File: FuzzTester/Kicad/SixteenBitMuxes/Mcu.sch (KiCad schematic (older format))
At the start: 20 parts, among them J10 Key Pad JST XH, J11 LCD JST XH, J12 Bypass Switch JST XH, J7 Boot Reset PinHeader, J8 SPI Test PinHeader, J9 SWD_PinHeader, U3 STM32F103C8Tx, Y1 8MHz

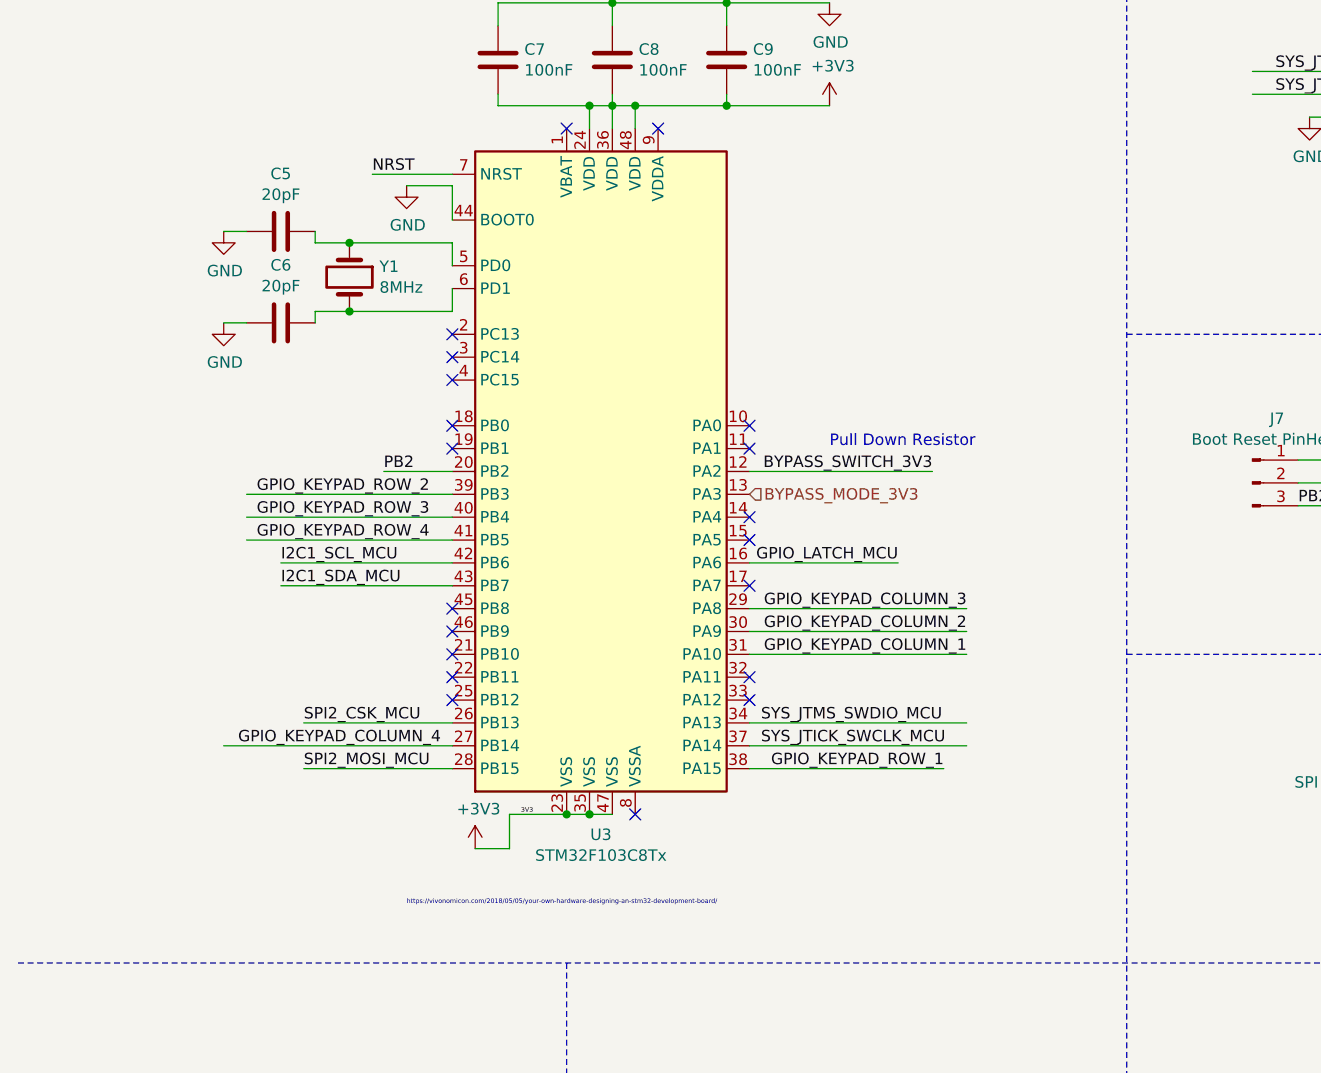
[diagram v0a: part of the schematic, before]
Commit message: Removed shift registers
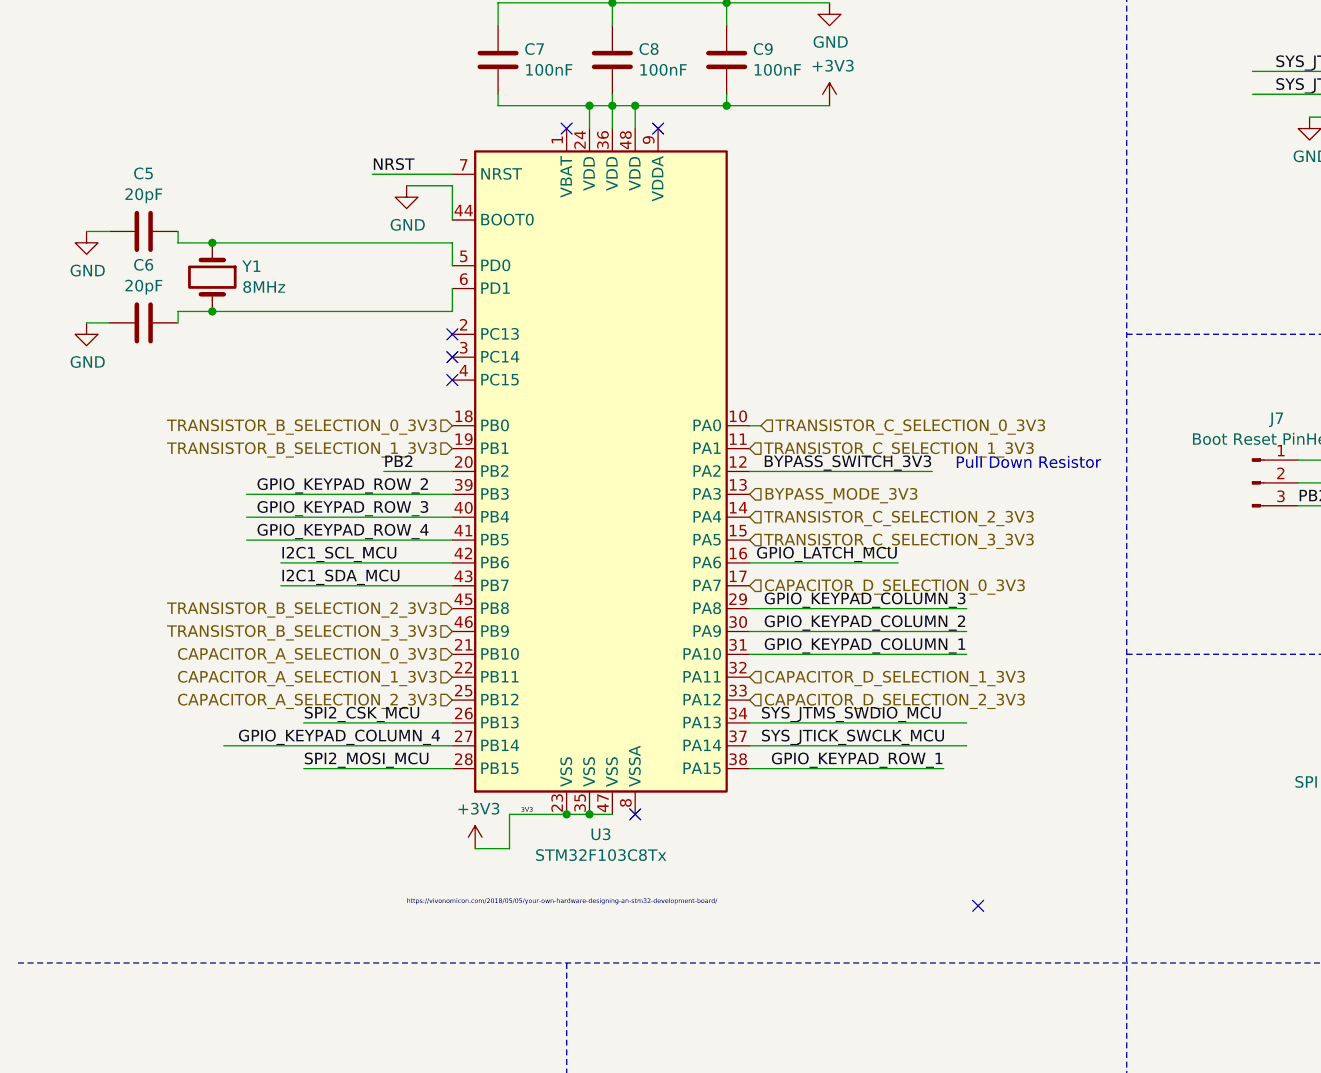
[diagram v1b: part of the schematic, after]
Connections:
- net labels added: CAPACITOR_A_SELECTION_0_3V3, CAPACITOR_A_SELECTION_1_3V3, CAPACITOR_A_SELECTION_2_3V3, CAPACITOR_D_SELECTION_0_3V3, CAPACITOR_D_SELECTION_1_3V3, CAPACITOR_D_SELECTION_2_3V3, TRANSISTOR_B_SELECTION_0_3V3, TRANSISTOR_B_SELECTION_1_3V3, TRANSISTOR_B_SELECTION_2_3V3, TRANSISTOR_B_SELECTION_3_3V3, TRANSISTOR_C_SELECTION_0_3V3, TRANSISTOR_C_SELECTION_1_3V3, TRANSISTOR_C_SELECTION_2_3V3, TRANSISTOR_C_SELECTION_3_3V3
- wire segments 93 -> 94
- no-connect marks 22 -> 9
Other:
- moved on the sheet: C5, C6, Y1
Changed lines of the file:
@@
 $Descr A4 11693 8268
 encoding utf-8
-Sheet 11 11
+Sheet 6 9
 Title "Guitar Pedal Effect Fuzz Digitally Controlled"
 Date "2020-04-07"
@@
 Comment4 "Micro Controller Unit and User Interface"
 $EndDescr
-$Comp
-L MCU_ST_STM32F1:STM32F103C8Tx U?
-U 1 1 5E8CE625
-P 3100 3050
-AR Path="/5E8CE625" Ref="U?"  Part="1"
-AR Path="/5E8BDF21/5E8CE625" Ref="U3"  Part="1"
-F 0 "U3" H 3050 1461 50  0000 C CNN
-F 1 "STM32F103C8Tx" H 3050 1370 50  0000 C CNN
-F 2 "Package_QFP:LQFP-48_7x7mm_P0.5mm" H 2500 1650 50  0001 R CNN
-F 3 "http://www.st.com/st-web-ui/static/active/en/resource/technical/document/datasheet/CD00161566.pdf" H 3100 3050 50  0001 C CNN
-	1    3100 3050
-	1    0    0    -1
-$EndComp
 $Comp
 L Device:C C?
@@
 Wire Wire Line
 	2650 4700 2650 4550
-Wire Wire Line
-	2900 4550 3000 4550
-Connection ~ 3000 4550
-Wire Wire Line
-	3000 4550 3100 4550
 Text Label 2700 4550 0    20   ~ 0
 3V3
@@
 L Device:Crystal Y?
 U 1 1 5E8CE662
-P 1950 2200
+P 1350 2200
 AR Path="/5E8CE662" Ref="Y?"  Part="1"
 AR Path="/5E8BDF21/5E8CE662" Ref="Y1"  Part="1"
-F 0 "Y1" V 1904 2331 50  0000 L CNN
-F 1 "8MHz" V 1995 2331 50  0000 L CNN
-F 2 "Crystal:Crystal_HC49-U_Vertical" H 1950 2200 50  0001 C CNN
-F 3 "~" H 1950 2200 50  0001 C CNN
-	1    1950 2200
+F 0 "Y1" V 1304 2331 50  0000 L CNN
+F 1 "8MHz" V 1395 2331 50  0000 L CNN
+F 2 "Crystal:Crystal_HC49-U_Vertical" H 1350 2200 50  0001 C CNN
+F 3 "~" H 1350 2200 50  0001 C CNN
+	1    1350 2200
 	0    1    1    0
 $EndComp
@@
 L Device:C C?
 U 1 1 5E8CE668
-P 1650 2000
+P 1050 2000
 AR Path="/5E8CE668" Ref="C?"  Part="1"
 AR Path="/5E8BDF21/5E8CE668" Ref="C5"  Part="1"
-F 0 "C5" V 1398 2000 50  0000 C CNN
-F 1 "20pF" V 1489 2000 50  0000 C CNN
-F 2 "Capacitor_SMD:C_0805_2012Metric_Pad1.15x1.40mm_HandSolder" H 1688 1850 50  0001 C CNN
-F 3 "~" H 1650 2000 50  0001 C CNN
-	1    1650 2000
+F 0 "C5" V 798 2000 50  0000 C CNN
+F 1 "20pF" V 889 2000 50  0000 C CNN
+F 2 "Capacitor_SMD:C_0805_2012Metric_Pad1.15x1.40mm_HandSolder" H 1088 1850 50  0001 C CNN
+F 3 "~" H 1050 2000 50  0001 C CNN
+	1    1050 2000
 	0    1    1    0
 $EndComp
@@
 L Device:C C?
 U 1 1 5E8CE66E
-P 1650 2400
+P 1050 2400
 AR Path="/5E8CE66E" Ref="C?"  Part="1"
 AR Path="/5E8BDF21/5E8CE66E" Ref="C6"  Part="1"
-F 0 "C6" V 1398 2400 50  0000 C CNN
-F 1 "20pF" V 1489 2400 50  0000 C CNN
-F 2 "Capacitor_SMD:C_0805_2012Metric_Pad1.15x1.40mm_HandSolder" H 1688 2250 50  0001 C CNN
-F 3 "~" H 1650 2400 50  0001 C CNN
-	1    1650 2400
+F 0 "C6" V 798 2400 50  0000 C CNN
+F 1 "20pF" V 889 2400 50  0000 C CNN
+F 2 "Capacitor_SMD:C_0805_2012Metric_Pad1.15x1.40mm_HandSolder" H 1088 2250 50  0001 C CNN
+F 3 "~" H 1050 2400 50  0001 C CNN
+	1    1050 2400
 	0    1    1    0
 $EndComp
@@
 	2400 2250 2400 2350
 Wire Wire Line
-	2400 2350 1950 2350
-Wire Wire Line
-	1800 2400 1800 2350
-Wire Wire Line
-	1800 2350 1950 2350
-Connection ~ 1950 2350
-Wire Wire Line
-	1800 2000 1800 2050
-Wire Wire Line
-	1800 2050 1950 2050
-Wire Wire Line
-	1950 2050 2400 2050
+	1200 2400 1200 2350
+Wire Wire Line
+	1200 2350 1350 2350
+Connection ~ 1350 2350
+Wire Wire Line
+	1200 2000 1200 2050
+Wire Wire Line
+	1200 2050 1350 2050
 Wire Wire Line
 	2400 2050 2400 2150
-Connection ~ 1950 2050
+Connection ~ 1350 2050
 $Comp
 L power:GND #PWR?
 U 1 1 5E8CE67E
-P 1400 2400
+P 800 2400
 AR Path="/5E8CE67E" Ref="#PWR?"  Part="1"
 AR Path="/5E8BDF21/5E8CE67E" Ref="#PWR018"  Part="1"
-F 0 "#PWR018" H 1400 2150 50  0001 C CNN
-F 1 "GND" H 1405 2227 50  0000 C CNN
-F 2 "" H 1400 2400 50  0001 C CNN
-F 3 "" H 1400 2400 50  0001 C CNN
-	1    1400 2400
+F 0 "#PWR018" H 800 2150 50  0001 C CNN
+F 1 "GND" H 805 2227 50  0000 C CNN
+F 2 "" H 800 2400 50  0001 C CNN
+F 3 "" H 800 2400 50  0001 C CNN
+	1    800  2400
 	1    0    0    -1
 $EndComp
@@
 L power:GND #PWR?
 U 1 1 5E8CE684
-P 1400 2000
+P 800 2000
 AR Path="/5E8CE684" Ref="#PWR?"  Part="1"
 AR Path="/5E8BDF21/5E8CE684" Ref="#PWR017"  Part="1"
-F 0 "#PWR017" H 1400 1750 50  0001 C CNN
-F 1 "GND" H 1405 1827 50  0000 C CNN
-F 2 "" H 1400 2000 50  0001 C CNN
-F 3 "" H 1400 2000 50  0001 C CNN
-	1    1400 2000
-	1    0    0    -1
-$EndComp
-Wire Wire Line
-	1400 2000 1500 2000
-Wire Wire Line
-	1400 2400 1500 2400
+F 0 "#PWR017" H 800 1750 50  0001 C CNN
+F 1 "GND" H 805 1827 50  0000 C CNN
+F 2 "" H 800 2000 50  0001 C CNN
+F 3 "" H 800 2000 50  0001 C CNN
+	1    800  2000
+	1    0    0    -1
+$EndComp
+Wire Wire Line
+	800  2000 900  2000
+Wire Wire Line
+	800  2400 900  2400
 Wire Wire Line
 	3600 1000 4050 1000
@@
 Wire Wire Line
 	2100 3050 2400 3050
-Wire Wire Line
-	2650 4550 2900 4550
-Connection ~ 2900 4550
 Text Notes 2200 900  0    50   ~ 10
 Micro Controller Unit\n\n\n
@@
 Text Notes 6350 1300 0    50   ~ 10
 SWD\n\n\n
-NoConn ~ 2400 2650
-NoConn ~ 2400 2550
-NoConn ~ 2400 2450
-NoConn ~ 2400 4050
-NoConn ~ 2400 3950
-NoConn ~ 2400 3850
-NoConn ~ 2400 3750
-NoConn ~ 2400 3650
-NoConn ~ 3700 4050
-NoConn ~ 3700 3950
-NoConn ~ 3700 3550
-NoConn ~ 3700 3350
-NoConn ~ 3700 3250
-NoConn ~ 3700 2950
-NoConn ~ 3700 2850
 NoConn ~ 2900 1550
 NoConn ~ 3300 1550
@@
 Wire Wire Line
 	8700 4400 9250 4400
-NoConn ~ 2400 2850
-Text Notes 4050 2950 0    50   ~ 0
+Text Notes 4600 3050 0    50   ~ 0
 Pull Down Resistor
 Text HLabel 3700 3150 2    50   Input ~ 0
@@
 Text Label 2350 4250 2    50   ~ 0
 GPIO_KEYPAD_COLUMN_4
-NoConn ~ 2400 2950
 Text Label 9500 1650 2    50   ~ 0
 GPIO_KEYPAD_ROW_4
@@
 Wire Wire Line
 	1650 3450 2400 3450
-$Comp
-L Device:R_Pack04 RN1
-U 1 1 5EA7B481
-P 1850 6700
-F 0 "RN1" V 1433 6700 50  0000 C CNN
-F 1 "R_Pack04" V 1524 6700 50  0000 C CNN
-F 2 "Resistor_SMD:R_Array_Convex_4x0603" V 2125 6700 50  0001 C CNN
-F 3 "~" H 1850 6700 50  0001 C CNN
-	1    1850 6700
-	0    1    1    0
-$EndComp
 $Comp
 L Device:R_Pack04 RN2
@@
 Text Label 850  6700 0    50   ~ 0
 SPI2_MOSI_MCU
-Text HLabel 2050 6700 2    50   Input ~ 0
-SPI2_MOSI
-Text HLabel 2050 6600 2    50   Input ~ 0
-SPI2_CSK
 Text Label 1750 4350 0    50   ~ 0
 SPI2_MOSI_MCU
@@
 Wire Wire Line
 	3700 3450 4350 3450
-Text Label 1500 6500 2    50   ~ 0
-GPIO_LATCH_MCU
-Text HLabel 2050 6500 2    50   Input ~ 0
-GPIO_LATCH
-Wire Wire Line
-	1650 6500 850  6500
-Wire Wire Line
-	850  6600 1650 6600
-Wire Wire Line
-	1650 6700 850  6700
 Wire Wire Line
 	3950 6800 3350 6800
@@
 Wire Wire Line
 	4350 6700 4700 6700
-NoConn ~ 1650 6800
-NoConn ~ 2050 6800
-Text Notes 1600 6250 0    50   ~ 10
-I2C CROSSTALK\n\n\n
 Text Notes 3800 6250 0    50   ~ 10
 SWDIO/I2C CROSSTALK\n\n\n
@@
 Wire Notes Line
 	500  5200 11200 5200
+Wire Wire Line
+	1350 2050 2400 2050
+Wire Wire Line
+	1350 2350 2400 2350
 Text Notes 1250 7050 0    50   ~ 0
 Check: Concave or Convex footprint
+Text Notes 1600 6250 0    50   ~ 10
+I2C CROSSTALK\n\n\n
+NoConn ~ 2050 6800
+NoConn ~ 1650 6800
+Wire Wire Line
+	1650 6700 850  6700
+Wire Wire Line
+	850  6600 1650 6600
+Wire Wire Line
+	1650 6500 850  6500
+Text HLabel 2050 6500 2    50   Input ~ 0
+GPIO_LATCH
+Text Label 1500 6500 2    50   ~ 0
+GPIO_LATCH_MCU
+Text HLabel 2050 6600 2    50   Input ~ 0
+SPI2_CSK
+Text HLabel 2050 6700 2    50   Input ~ 0
+SPI2_MOSI
+$Comp
+L Device:R_Pack04 RN1
+U 1 1 5EA7B481
+P 1850 6700
+F 0 "RN1" V 1433 6700 50  0000 C CNN
+F 1 "R_Pack04" V 1524 6700 50  0000 C CNN
+F 2 "Resistor_SMD:R_Array_Convex_4x0603" V 2125 6700 50  0001 C CNN
+F 3 "~" H 1850 6700 50  0001 C CNN
+	1    1850 6700
+	0    1    1    0
+$EndComp
+Wire Wire Line
+	3000 4550 3100 4550
+Connection ~ 3000 4550
+Wire Wire Line
+	2650 4550 2900 4550
+Wire Wire Line
+	2900 4550 3000 4550
+Connection ~ 2900 4550
+$Comp
+L MCU_ST_STM32F1:STM32F103C8Tx U?
+U 1 1 5E8CE625
+P 3100 3050
+AR Path="/5E8CE625" Ref="U?"  Part="1"
+AR Path="/5E8BDF21/5E8CE625" Ref="U3"  Part="1"
+F 0 "U3" H 3050 1461 50  0000 C CNN
+F 1 "STM32F103C8Tx" H 3050 1370 50  0000 C CNN
+F 2 "Package_QFP:LQFP-48_7x7mm_P0.5mm" H 2500 1650 50  0001 R CNN
+F 3 "http://www.st.com/st-web-ui/static/active/en/resource/technical/document/datasheet/CD00161566.pdf" H 3100 3050 50  0001 C CNN
+	1    3100 3050
+	1    0    0    -1
+$EndComp
+NoConn ~ 2400 2450
+NoConn ~ 2400 2550
+NoConn ~ 2400 2650
+NoConn ~ 4700 4950
+Text HLabel 2400 2850 0    50   Input ~ 0
+TRANSISTOR_B_SELECTION_0_3V3
+Text HLabel 2400 2950 0    50   Input ~ 0
+TRANSISTOR_B_SELECTION_1_3V3
+Text HLabel 2400 3650 0    50   Input ~ 0
+TRANSISTOR_B_SELECTION_2_3V3
+Text HLabel 2400 3750 0    50   Input ~ 0
+TRANSISTOR_B_SELECTION_3_3V3
+Text HLabel 2400 3850 0    50   Input ~ 0
+CAPACITOR_A_SELECTION_0_3V3
+Text HLabel 2400 3950 0    50   Input ~ 0
+CAPACITOR_A_SELECTION_1_3V3
+Text HLabel 2400 4050 0    50   Input ~ 0
+CAPACITOR_A_SELECTION_2_3V3
+Text HLabel 3750 2850 2    50   Input ~ 0
+TRANSISTOR_C_SELECTION_0_3V3
+Text HLabel 3700 2950 2    50   Input ~ 0
+TRANSISTOR_C_SELECTION_1_3V3
+Text HLabel 3700 3250 2    50   Input ~ 0
+TRANSISTOR_C_SELECTION_2_3V3
+Text HLabel 3700 3350 2    50   Input ~ 0
+TRANSISTOR_C_SELECTION_3_3V3
+Text HLabel 3700 3550 2    50   Input ~ 0
+CAPACITOR_D_SELECTION_0_3V3
+Text HLabel 3700 3950 2    50   Input ~ 0
+CAPACITOR_D_SELECTION_1_3V3
+Text HLabel 3700 4050 2    50   Input ~ 0
+CAPACITOR_D_SELECTION_2_3V3
+Wire Wire Line
+	3700 2850 3750 2850
 $EndSCHEMATC
